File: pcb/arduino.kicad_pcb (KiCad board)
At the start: 2 copper layers, 46 parts, among them SW1 SW_DIP_x08, SW2 SW_DIP_x08, U1 ATMEGA328-PU

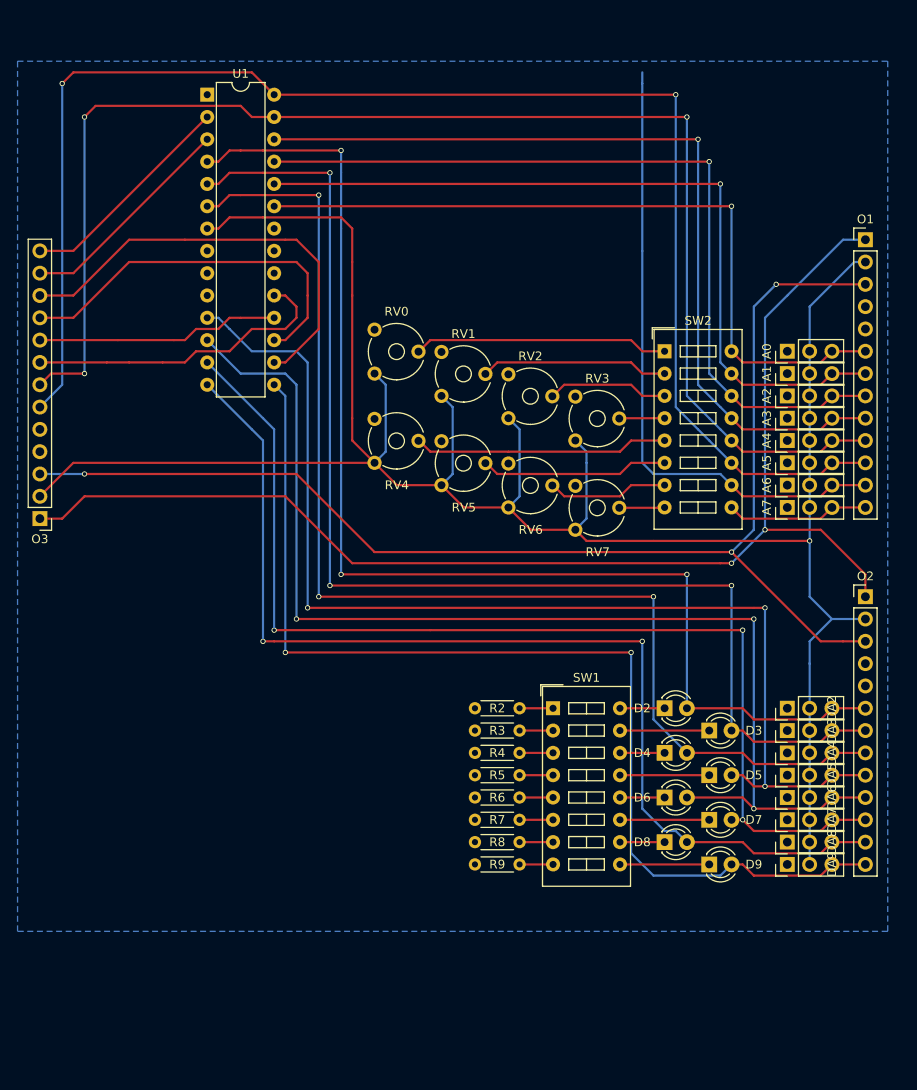
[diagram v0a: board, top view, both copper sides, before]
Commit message: Added Pro Mini and Nano boards, and power connector.
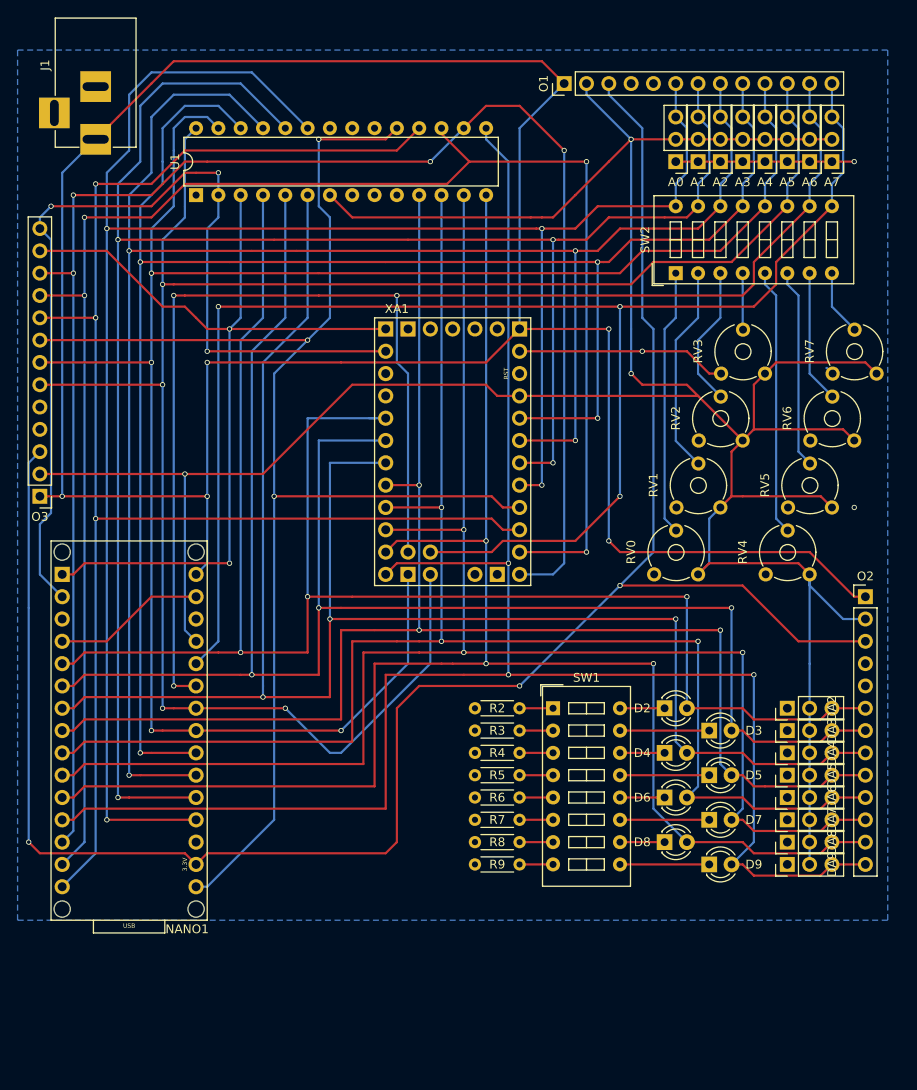
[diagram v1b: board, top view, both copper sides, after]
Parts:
- added J1: Conn_Coaxial_Power, Connectors:BARREL_JACK, F.Cu at (69.8, 24.1)
- added NANO1: Arduino_Nano_Socket, Arduino:Arduino_Nano_Socket, F.Cu at (73.7, 113.0)
- added XA1: Arduino_Mini_03_Socket, Arduino:Arduino_Mini_Socket, F.Cu at (101.6, 74.9)
- moved RV4 51.1 mm to (151.1, 73.7), turned to 90 degrees
- moved RV5 44.5 mm to (153.7, 66.0), turned to 90 degrees
- moved RV0 43.3 mm to (138.4, 73.7), turned to 90 degrees
- moved RV6 40.1 mm to (156.2, 58.4), turned to 90 degrees
- moved A7 39.7 mm to (153.7, 26.7), turned to 180 degrees
- moved RV7 38.6 mm to (158.8, 50.8), turned to 90 degrees
- moved O1 38.6 mm to (123.2, 17.8), turned to 90 degrees
- moved A6 36.9 mm to (151.1, 26.7), turned to 180 degrees
- moved A5 34.3 mm to (148.6, 26.7), turned to 180 degrees
- moved RV1 34.2 mm to (141.0, 66.0), turned to 90 degrees
- moved A4 31.9 mm to (146.1, 26.7), turned to 180 degrees
- moved A3 29.6 mm to (143.5, 26.7), turned to 180 degrees
- moved A2 27.7 mm to (141.0, 26.7), turned to 180 degrees
- moved RV2 26.8 mm to (143.5, 58.4), turned to 90 degrees
- moved A1 26.2 mm to (138.4, 26.7), turned to 180 degrees
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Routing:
- net /A7: track 16.3 -> 178.6 mm, vias 0 -> 3
- net /D11: track 43.6 -> 196.8 mm, vias 0 -> 4
- net /D12: track 27.7 -> 176.2 mm, vias 0 -> 3
- net /A0: track 84.9 -> 230.4 mm, vias 1 -> 4
- net /D10: track 49.7 -> 193.4 mm, vias 0 -> 4
- net /VIN: track 143.7 -> 277.3 mm, vias 2 -> 5
- net /A1: track 89.2 -> 220.2 mm, vias 1 -> 4
- net /D13: track 35.7 -> 161.7 mm, vias 0 -> 3
- net /A2: track 93.5 -> 211.3 mm, vias 1 -> 4
- net /A3: track 97.9 -> 202.4 mm, vias 1 -> 4
- net /A6: track 72.0 -> 169.8 mm, vias 0 -> 3
- net /D9: track 122.5 -> 211.2 mm, vias 2 -> 3
- net /D0: track 25.4 -> 109.5 mm, vias 0 -> 3
- net /3V3: track 144.6 -> 226.8 mm
- net /D1: track 25.4 -> 105.1 mm, vias 0 -> 2
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
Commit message: Made more room for bare AT chip's crystal.
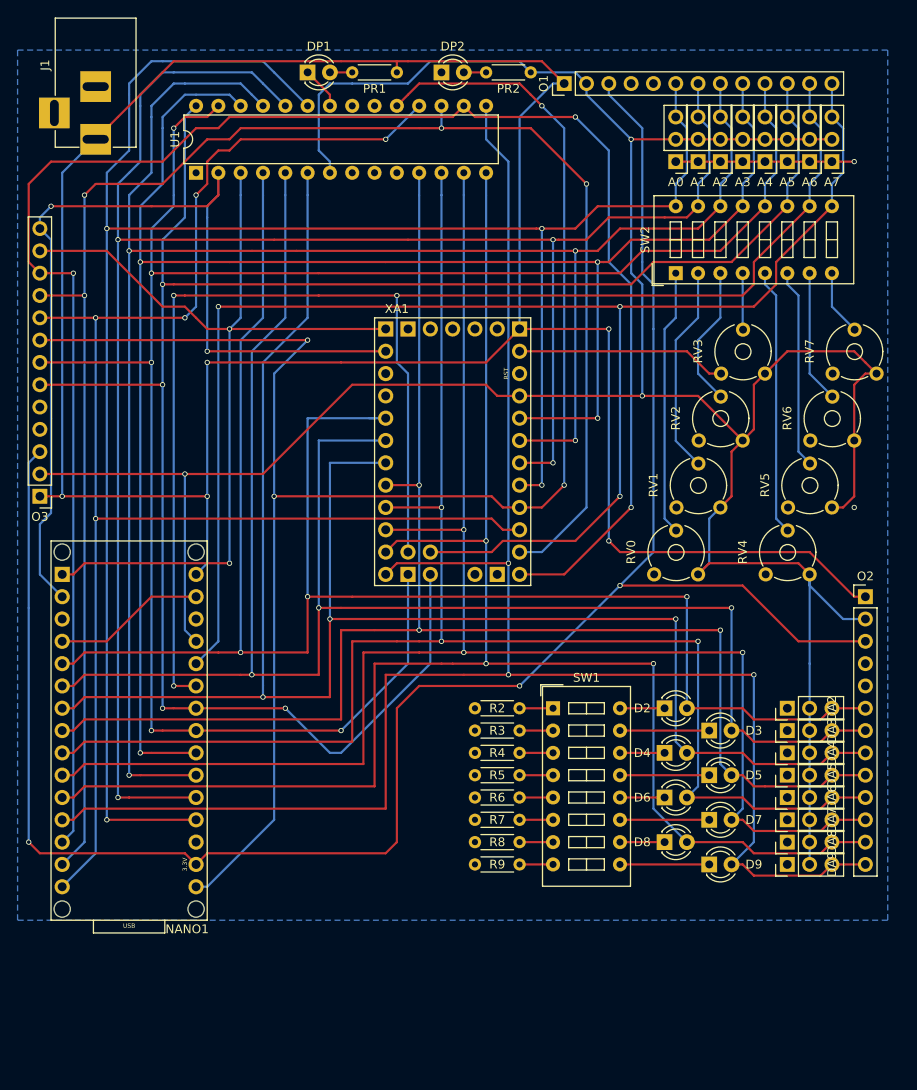
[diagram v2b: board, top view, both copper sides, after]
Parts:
- added DP1: LED, LEDs:LED_D3.0mm, F.Cu at (94.0, 16.5)
- added DP2: LED, LEDs:LED_D3.0mm, F.Cu at (109.2, 16.5)
- added PR1: R, Resistors_THT:R_Axial_DIN0204_L3.6mm_D1.6mm_P5.08mm_Horizontal, F.Cu at (104.1, 16.5)
- added PR2: R, Resistors_THT:R_Axial_DIN0204_L3.6mm_D1.6mm_P5.08mm_Horizontal, F.Cu at (119.4, 16.5)
- moved U1 2.54 mm to (81.3, 27.9)
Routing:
- net /D13: track 161.7 -> 196.8 mm, vias 3 -> 4
- net /D10: track 193.4 -> 209.2 mm, vias 4 -> 3
- net /VCC: track 331.8 -> 325.6 mm
- net Earth: track 61.7 -> 66.5 mm, vias 2 -> 1
- net /D4: track 199.8 -> 202.3 mm
- net Net-(DP1-Pad2): track 0.00 -> 2.54 mm
- net /D1: track 105.1 -> 107.6 mm
- net Net-(DP2-Pad2): track 0.00 -> 2.54 mm
- net /D9: track 211.2 -> 213.8 mm
- net /D8: track 190.4 -> 192.9 mm
- net /D7: track 187.5 -> 190.1 mm
- net /D6: track 181.2 -> 183.7 mm
- net /D5: track 172.3 -> 174.8 mm
- net /D3: track 197.5 -> 200.0 mm
- net /D2: track 195.0 -> 197.6 mm
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
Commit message: Added edge cuts. Plus minor tweaks.
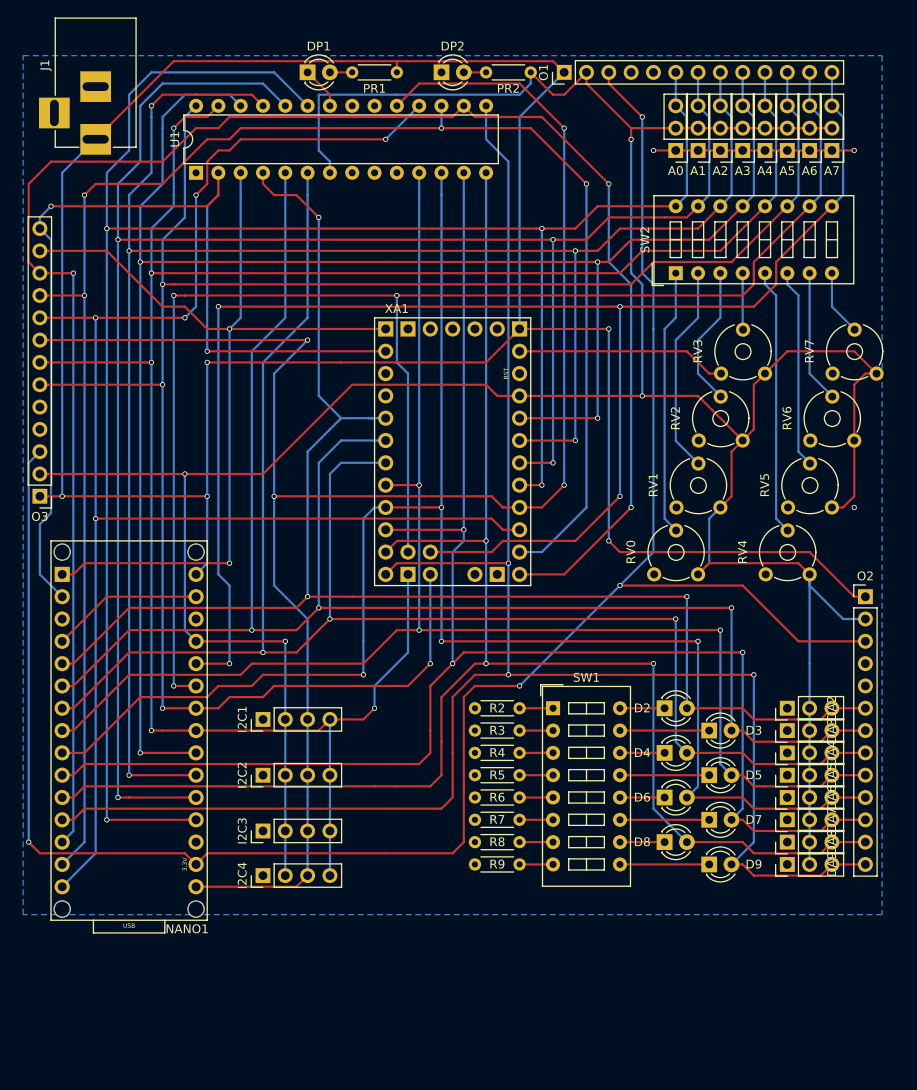
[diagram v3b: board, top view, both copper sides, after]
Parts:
- added I2C1: I2CHeader, Pin_Headers:Pin_Header_Straight_1x04_Pitch2.54mm, F.Cu at (88.9, 90.2)
- added I2C2: I2CHeader, Pin_Headers:Pin_Header_Straight_1x04_Pitch2.54mm, F.Cu at (88.9, 96.5)
- added I2C3: I2CHeader, Pin_Headers:Pin_Header_Straight_1x04_Pitch2.54mm, F.Cu at (88.9, 102.9)
- added I2C4: I2CHeader, Pin_Headers:Pin_Header_Straight_1x04_Pitch2.54mm, F.Cu at (88.9, 108.0)
- moved A0 1.27 mm to (135.9, 25.4)
- moved A1 1.27 mm to (138.4, 25.4)
- moved A2 1.27 mm to (141.0, 25.4)
- moved A3 1.27 mm to (143.5, 25.4)
- moved A4 1.27 mm to (146.1, 25.4)
- moved A5 1.27 mm to (148.6, 25.4)
- moved A6 1.27 mm to (151.1, 25.4)
- moved A7 1.27 mm to (153.7, 25.4)
- moved O1 1.27 mm to (123.2, 16.5)
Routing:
- net /VCC: track 325.6 -> 365.0 mm, vias 3 -> 4
- net /D2: track 197.6 -> 169.1 mm
- net /A4: track 219.0 -> 238.8 mm
- net /D4: track 202.3 -> 191.3 mm
- net /D3: track 200.0 -> 189.0 mm
- net /D13: track 196.8 -> 205.9 mm
- net /D5: track 174.8 -> 168.9 mm
- net /A7: track 178.6 -> 183.2 mm, vias 3 -> 4
- net /D6: track 183.7 -> 187.4 mm, vias 3 -> 4
- net /D8: track 192.9 -> 189.9 mm
- net /A5: track 220.9 -> 218.0 mm
- net Earth: track 66.5 -> 69.1 mm, vias 1 -> 2
- net /D10: track 209.2 -> 206.9 mm
- net /D9: track 213.8 -> 211.5 mm
- net /3V3: track 226.8 -> 228.8 mm, vias 3 -> 4
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
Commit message: Reworked the circuit from scratch.
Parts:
- removed DP1, DP2: LED, LEDs:LED_D3.0mm
- removed SW2: SW_DIP_x08, Buttons_Switches_THT:SW_DIP_x8_W7.62mm_Slide
- added ?: M3, Mounting_Holes:MountingHole_3.2mm_M3, F.Cu at (65.4, 34.3)
- added ?: M3, Mounting_Holes:MountingHole_3.2mm_M3, F.Cu at (158.1, 34.3)
- added ?: M3, Mounting_Holes:MountingHole_3.2mm_M3, F.Cu at (158.1, 127.0)
- added ?: M3, Mounting_Holes:MountingHole_3.2mm_M3, F.Cu at (65.4, 127.0)
- added C1: 100nF, Capacitors_THT:C_Disc_D3.0mm_W1.6mm_P2.50mm, F.Cu at (143.5, 73.7)
- added C2: 22pF, Capacitors_THT:C_Disc_D3.0mm_W1.6mm_P2.50mm, F.Cu at (143.5, 86.4)
- added C3: 22pF, Capacitors_THT:C_Disc_D3.0mm_W1.6mm_P2.50mm, F.Cu at (148.6, 86.4)
- added D10: DATA, Pin_Headers:Pin_Header_Straight_1x03_Pitch2.54mm, F.Cu at (73.7, 114.3)
- added FT1: FTDI, Pin_Headers:Pin_Header_Straight_1x06_Pitch2.54mm, F.Cu at (85.1, 69.8)
- added H1: Headers8L, Pin_Headers:Pin_Header_Straight_1x08_Pitch2.54mm, F.Cu at (134.6, 48.3)
- added H2: Headers8, Pin_Headers:Pin_Header_Straight_1x08_Pitch2.54mm, F.Cu at (134.6, 45.7)
- added H3: Headers8L, Pin_Headers:Pin_Header_Straight_1x08_Pitch2.54mm, F.Cu at (133.3, 102.9)
- added H4: Headers8, Pin_Headers:Pin_Header_Straight_1x08_Pitch2.54mm, F.Cu at (135.9, 102.9)
- added LED1: FTDI, LEDs:LED_D3.0mm, F.Cu at (99.1, 34.3)
- added LED2: VCC, LEDs:LED_D3.0mm, F.Cu at (91.4, 34.3)
- added LED3: BRD, LEDs:LED_D3.0mm, F.Cu at (106.7, 34.3)
- added LED4: VIN, LEDs:LED_D3.0mm, F.Cu at (83.8, 34.3)
- added MISO1: DATA, Pin_Headers:Pin_Header_Straight_1x03_Pitch2.54mm, F.Cu at (73.7, 109.2)
- added MOSI1: DATA, Pin_Headers:Pin_Header_Straight_1x03_Pitch2.54mm, F.Cu at (73.7, 111.8)
- added PR3: R, Resistors_THT:R_Axial_DIN0204_L3.6mm_D1.6mm_P5.08mm_Horizontal, F.Cu at (104.1, 38.1)
- added PR4: R, Resistors_THT:R_Axial_DIN0204_L3.6mm_D1.6mm_P5.08mm_Horizontal, F.Cu at (96.5, 38.1)
- added R1: 10K, Resistors_THT:R_Axial_DIN0204_L3.6mm_D1.6mm_P5.08mm_Horizontal, F.Cu at (132.1, 86.4)
- added RESET1: SW_Push, Buttons_Switches_THT:SW_PUSH_6mm, F.Cu at (120.7, 91.4)
- added RXD1: DATA, Pin_Headers:Pin_Header_Straight_1x03_Pitch2.54mm, F.Cu at (73.7, 119.4)
- added SCK1: DATA, Pin_Headers:Pin_Header_Straight_1x03_Pitch2.54mm, F.Cu at (73.7, 106.7)
- added SCL1: DATA, Pin_Headers:Pin_Header_Straight_1x03_Pitch2.54mm, F.Cu at (73.7, 101.6)
- added SDA1: DATA, Pin_Headers:Pin_Header_Straight_1x03_Pitch2.54mm, F.Cu at (73.7, 104.1)
- added TXD1: DATA, Pin_Headers:Pin_Header_Straight_1x03_Pitch2.54mm, F.Cu at (73.7, 116.8)
- added U2: L7805, Power_Integrations:TO-220, F.Cu at (85.7, 43.2)
- added Y1: 16MHz, Crystals:Resonator-2pin_w6.0mm_h3.0mm, F.Cu at (147.3, 90.2)
- D2, D3, D4, D5, D6, D7, D8, D9: footprint LEDs:LED_D3.0mm -> LEDs:LED_PLCC_2835
- NANO1: footprint Arduino:Arduino_Nano_Socket -> Arduino:Arduino_Nano
- SW1: value SW_DIP_x08 -> SW_SPDT; footprint Buttons_Switches_THT:SW_DIP_x8_W7.62mm_Slide -> Buttons_Switches_THT:SW_CuK_JS202011CQN_DPDT_Straight
- XA1: value Arduino_Mini_03_Socket -> Arduino_ProMini; footprint Arduino:Arduino_Mini_Socket -> Arduino:Arduino_ProMini
- moved U1 69.8 mm to (123.2, 83.8)
- moved SW1 52.4 mm to (101.6, 40.6)
- moved I2C4 34.2 mm to (71.1, 78.7)
- moved NANO1 29.6 mm to (99.1, 128.3)
- moved I2C2 28.0 mm to (71.1, 74.9)
- moved I2C3 27.0 mm to (71.1, 82.5)
- moved PR1 26.4 mm to (88.9, 38.1), turned to 90 degrees
- moved O3 24.1 mm to (64.1, 88.9), turned to 0 degrees
- moved J1 21.4 mm to (74.3, 45.1)
- moved R2 18.9 mm to (130.8, 102.9)
- moved R3 18.9 mm to (130.8, 105.4)
- moved R4 18.9 mm to (130.8, 108.0)
- moved R5 18.9 mm to (130.8, 110.5)
- moved R6 18.9 mm to (130.8, 113.0)
- moved R7 18.9 mm to (130.8, 115.6)
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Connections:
- I2C1 pad 3: /D13 -> /A5
- I2C2 pad 3: /D13 -> /A5
- I2C3 pad 3: /D13 -> /A5
- I2C4 pad 3: /D13 -> /A5
- PR2 pad 1: /VCC -> Net-(LED3-Pad2)
- PR2 pad 2: Net-(DP2-Pad2) -> Net-(PR2-Pad2)
- R2 pad 1: Net-(R2-Pad1) -> Net-(H3-Pad1)
- R3 pad 1: Net-(R3-Pad1) -> Net-(H3-Pad2)
- R4 pad 1: Net-(R4-Pad1) -> Net-(H3-Pad3)
- R5 pad 1: Net-(R5-Pad1) -> Net-(H3-Pad4)
- R6 pad 1: Net-(R6-Pad1) -> Net-(H3-Pad5)
- R7 pad 1: Net-(R7-Pad1) -> Net-(H3-Pad6)
- R8 pad 1: Net-(R8-Pad1) -> Net-(H3-Pad7)
- R9 pad 1: Net-(R9-Pad1) -> Net-(H3-Pad8)
- RV7 pad 3: Earth -> (no net)
- SW1 pad 1: Net-(R2-Pad1) -> Net-(FT1-Pad3)
- SW1 pad 2: Net-(R3-Pad1) -> /VCC
- SW1 pad 3: Net-(R4-Pad1) -> Net-(PR2-Pad2)
- SW1 pad 4: Net-(R5-Pad1) -> (no net)
- SW1 pad 5: Net-(R6-Pad1) -> (no net)
- SW1 pad 6: Net-(R7-Pad1) -> (no net)
- U1 pad 1: (no net) -> /RESET
- U1 pad 10: (no net) -> Net-(C3-Pad2)
- U1 pad 20: (no net) -> /AVCC
- U1 pad 9: (no net) -> Net-(C2-Pad1)
- XA1 pad GND3: (no net) -> Net-(XA1-PadGND3)
- XA1 pad L2: (no net) -> /RESET
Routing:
- net /VCC: track 365.0 -> 475.6 mm, vias 4 -> 6
- net /RESET: track 0.00 -> 104.1 mm, vias 0 -> 1
- net /A0: track 230.6 -> 147.8 mm, vias 4 -> 2
- net /A1: track 220.4 -> 142.1 mm, vias 4 -> 3
- net /A2: track 212.3 -> 139.2 mm, vias 5 -> 3
- net /A7: track 183.2 -> 113.2 mm, vias 4 -> 1
- net /D10: track 206.9 -> 139.2 mm, vias 3 -> 6
- net /A3: track 204.4 -> 136.7 mm
- net /D13: track 205.9 -> 145.1 mm, vias 4 -> 1
- net /A6: track 171.1 -> 116.2 mm, vias 3 -> 2
- net /D9: track 211.5 -> 161.2 mm, vias 3 -> 4
- net /D11: track 194.4 -> 144.8 mm, vias 4 -> 5
- net Net-(FT1-Pad3): track 0.00 -> 41.1 mm, vias 0 -> 1
- net /D8: track 189.9 -> 149.9 mm, vias 3 -> 4
- net /D12: track 177.2 -> 138.6 mm, vias 5 -> 4
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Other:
- board text added: "ANALOG IO"
- board text added: "ATMEGA 328"
- board text added: "Arduino Playground V1.0"
- board text added: "BRD"
- board text added: "DIGITAL IO"
- board text added: "Enable LEDs"
- board text added: "Enable Pots"
- board text added: "FTDI"
- board text added: "GND"
- board text added: "NANO"
- board text added: "PRO MINI"
- board text added: "SCL"
- board text added: "SDA"
- board text added: "SERIAL IO"
- board text added: "VCC"
- board text added: "VIN"

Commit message: Tidy up - Note, there is a problem with VIN.
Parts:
- moved FT1 1.91 mm to (85.1, 67.9)
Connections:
- NANO1 pad RST2: (no net) -> /RESET
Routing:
- net /VIN: track 241.6 -> 232.4 mm, vias 8 -> 7
- net /RESET: track 104.1 -> 109.5 mm, vias 1 -> 2
- net Net-(FT1-Pad3): track 41.1 -> 36.0 mm, vias 1 -> 0
- net /3V3: track 259.9 -> 255.8 mm
- net /A3: track 136.7 -> 139.2 mm
- net /A4: track 268.4 -> 270.0 mm
- net Earth: track 58.8 -> 57.2 mm
- net /A2: track 139.2 -> 140.7 mm
- net /D12: track 138.6 -> 137.1 mm
- net /A1: track 142.1 -> 143.6 mm
- net /A0: track 147.8 -> 149.3 mm
- net /D11: track 144.8 -> 145.9 mm
- net /D2: track 132.6 -> 131.6 mm, vias 6 -> 4
- net /D0: track 137.8 -> 137.0 mm
- net /D13: track 145.1 -> 144.4 mm
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
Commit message: More tweaking of the layout.
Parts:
- moved FT1 2.01 mm to (87.0, 67.3)
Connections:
- NANO1 pad VIN: /VIN -> (no net)
- XA1 pad L2: /RESET -> (no net)
- XA1 pad RST2: (no net) -> /RESET
- XA1 pad VIN: /VIN -> (no net)
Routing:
- net /VIN: track 232.4 -> 214.7 mm, vias 7 -> 5
- net /RESET: track 109.5 -> 117.5 mm, vias 2 -> 4
- net /3V3: track 255.8 -> 249.8 mm
- net /D10: track 139.0 -> 133.1 mm, vias 6 -> 5
- net /D3: track 153.5 -> 149.8 mm
- net Earth: track 57.2 -> 54.1 mm, vias 1 -> 0
- net /D4: track 156.4 -> 153.4 mm
- net /D0: track 137.0 -> 134.4 mm, vias 3 -> 5
- net /D5: track 154.1 -> 151.9 mm
- net /VCC: track 475.6 -> 477.3 mm, vias 6 -> 5
- net /D11: track 145.9 -> 146.6 mm
- net /D12: track 137.1 -> 137.8 mm
- net Net-(FT1-Pad3): track 36.0 -> 36.7 mm
- net /D13: track 144.4 -> 144.7 mm, vias 1 -> 2
- net /D1: track 134.4 -> 134.6 mm, vias 3 -> 4
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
